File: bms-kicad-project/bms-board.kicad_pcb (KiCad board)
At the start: 4 copper layers, 218 parts, among them J1 12402012E212A, J2 DEBUG, J3 Conn_02x18_Odd_Even, J4 Conn_02x18_Odd_Even, Q1 BSS308PE_H6327, Q10 BSS308PE_H6327, Q11 BSS308PE_H6327, Q12 BSS308PE_H6327, Q13 BSS308PE_H6327, Q2 BSS308PE_H6327, Q3 BSS308PE_H6327, Q4 BSS308PE_H6327, Q5 BSS308PE_H6327, Q6 BSS308PE_H6327, Q7 BSS308PE_H6327, Q8 BSS308PE_H6327, Q9 BSS308PE_H6327, SW1 KMR223G LFG, SW2 KMR223G LFG, U1 LTC6804-2, U2 W25Q128JVSIQ TR, U3 NCP1117ST33T3G, U4 RP2040, U5 SIC461ED-T1-GE3, X1 ABM8-272-T3

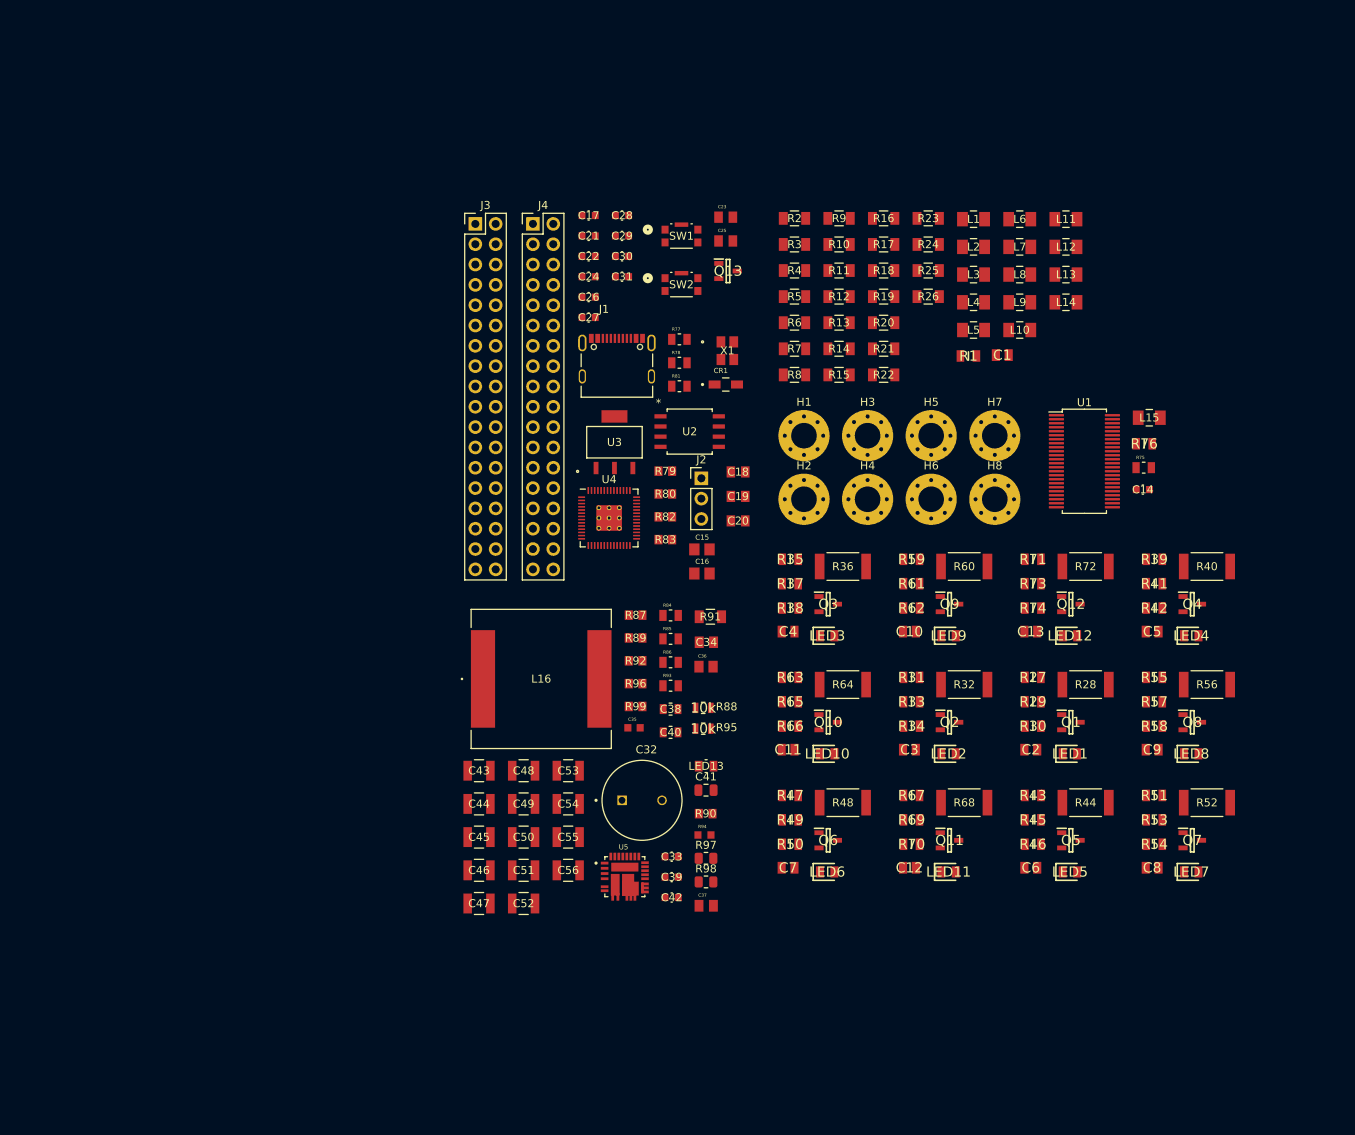
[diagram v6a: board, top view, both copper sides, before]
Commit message: Feature/current sensor (#17)
* feat: making sure my git still works

* feat: figured out battery stack monitor V+ biasing. Refer to task 5 on the punchlist for more details.

* feat: swapped out battery<->18V diode for cheaper alternative

* feat: started a new sheet for external connections and added current sensor

* feat: made a placeholder label to connect current sensor to LTC6811 GPIO

* feat: added remaining connectors to component library

* Wired up most external connections

* feat: Just shifting a few things around
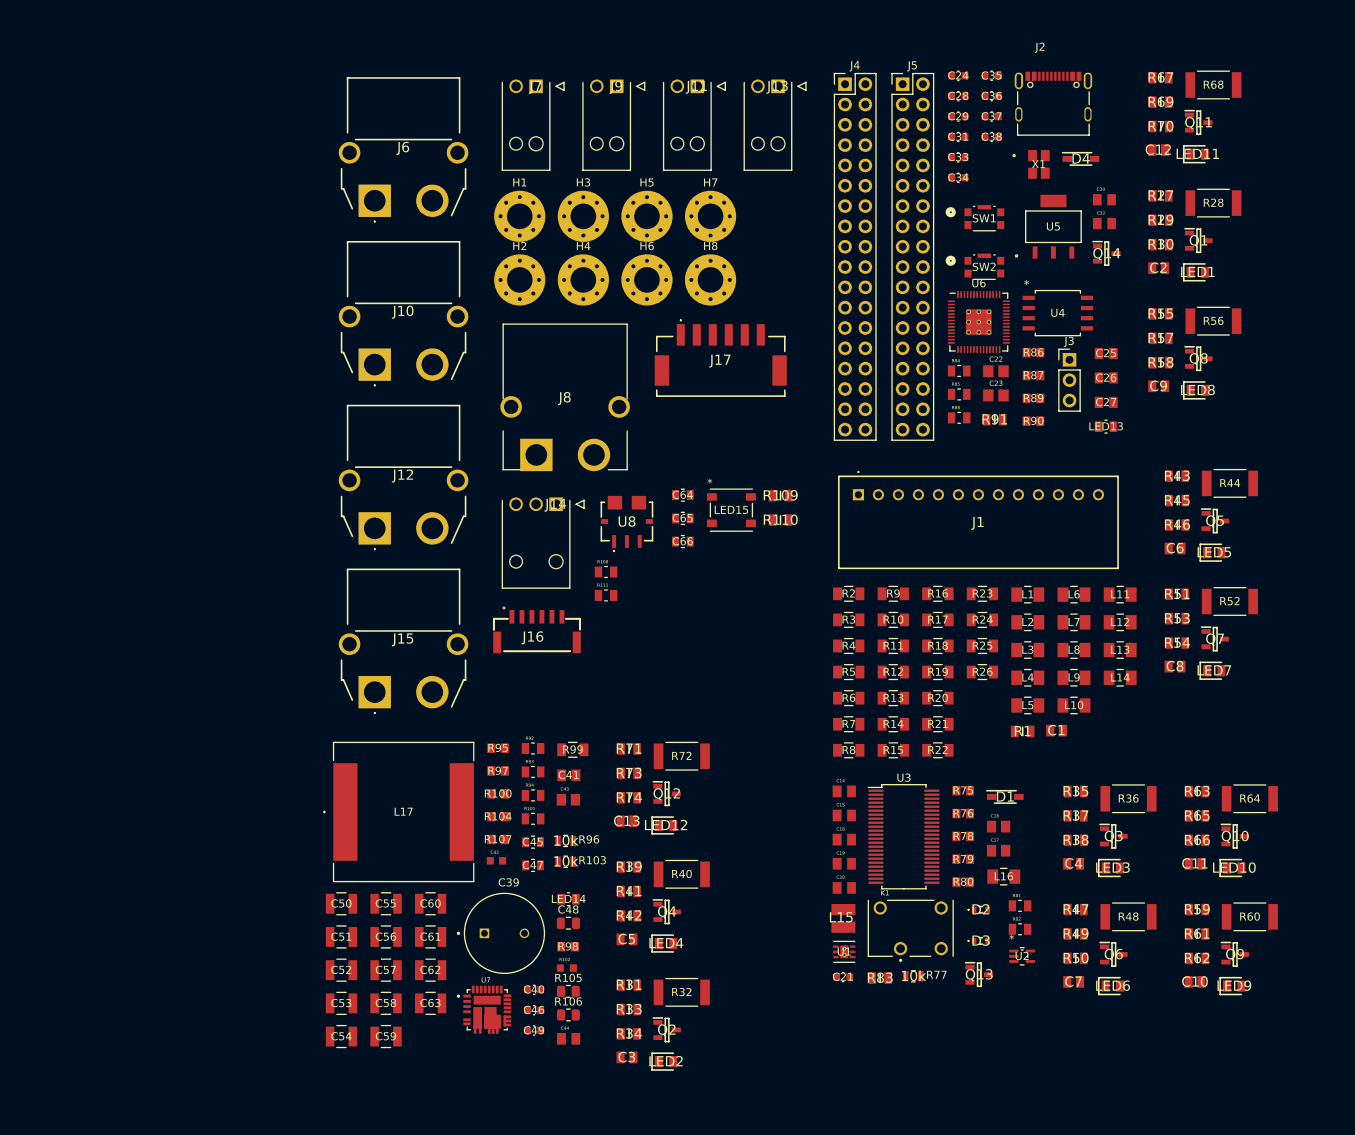
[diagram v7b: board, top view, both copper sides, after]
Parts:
- removed CR1: MBR120VLSFT1G, FixedWing:DIOM3616X98N
- added C57: 47u, FixedWing:G-32_MUR, F.Cu at (75.9, 148.3)
- added C58: 47u, FixedWing:G-32_MUR, F.Cu at (75.9, 152.5)
- added C59: 47u, FixedWing:G-32_MUR, F.Cu at (75.9, 156.6)
- added C60: 47u, FixedWing:G-32_MUR, F.Cu at (81.4, 140.0)
- added C61: 47u, FixedWing:G-32_MUR, F.Cu at (81.4, 144.2)
- added C62: 47u, FixedWing:G-32_MUR, F.Cu at (81.4, 148.3)
- added C63: 47u, FixedWing:G-32_MUR, F.Cu at (81.4, 152.5)
- added C64: 0.1µ, FixedWing:G-21_MUR, F.Cu at (113.0, 88.9)
- added C65: 1.5n, FixedWing:G-21_MUR, F.Cu at (113.0, 91.8)
- added C66: 0.1µ, FixedWing:G-21_MUR, F.Cu at (113.0, 94.7)
- added D1: B130LAW-7-F, FixedWing:SOD3716X145N, F.Cu at (153.3, 126.7)
- added D2: 1N4448X-TP, FixedWing:1N4448XTP, F.Cu at (150.2, 140.8)
- added D3: 1N4448X-TP, FixedWing:1N4448XTP, F.Cu at (150.2, 144.7)
- added D4: B130LAW-7-F, FixedWing:SOD3716X145N, F.Cu at (162.7, 46.9)
- added J10: XT60PW-F, FixedWing:XT60PWF, F.Cu at (74.5, 72.6)
- added J11: 1053131302, FixedWing:105313YY02, F.Cu at (114.8, 37.8)
- added J12: XT60PW-F, FixedWing:XT60PWF, F.Cu at (74.5, 93.1)
- added J13: 1053131302, FixedWing:105313YY02, F.Cu at (124.9, 37.8)
- added J14: 1053131303, FixedWing:105313YY03, F.Cu at (97.1, 90.1)
- added J15: XT60PW-F, FixedWing:XT60PWF, F.Cu at (74.5, 113.6)
- added J16: SM06B-GHS-TB, FixedWing:SM06B-GHS-TB, F.Cu at (89.4, 108.4)
- added J17: 5024940670, FixedWing:5024940670, F.Cu at (117.7, 72.7)
- added J5: Conn_02x18_Odd_Even, Connector_PinHeader_2.54mm:PinHeader_2x18_P2.54mm_Vertical, F.Cu at (140.4, 37.6)
- added J6: XT60PW-F, FixedWing:XT60PWF, F.Cu at (74.5, 52.1)
- added J7: 1053131302, FixedWing:105313YY02, F.Cu at (94.6, 37.8)
- added J8: XT60PW-M, FixedWing:XT60PWM, F.Cu at (98.3, 83.9)
- added J9: 1053131302, FixedWing:105313YY02, F.Cu at (104.7, 37.8)
- added K1: G6L-1P_DC5, FixedWing:RELAY_G6L-1P_DC5, F.Cu at (141.5, 143.1)
- added L17: 5.6u, FixedWing:IND_IHLP-6767GZ_VIS, F.Cu at (78.1, 128.5)
- added LED14: LTST-C170KGKT, FixedWing:LED_LTST-C170KGKT_LTO, F.Cu at (98.7, 139.4)
- added LED15: COM-16347, FixedWing:COM-16347_SPK, F.Cu at (119.0, 90.8)
- added Q14: BSS308PE_H6327, FixedWing:SOT95P260X110-3N, F.Cu at (166.0, 58.7)
- added R100: 1k, FixedWing:RC0805N_YAG, F.Cu at (89.9, 126.3)
- added R101: 93.1k, FixedWing:RESC2012X60N, F.Cu at (94.2, 129.4)
- added R102: 3.3, FixedWing:RESC1608X55N, F.Cu at (98.5, 148.0)
- added R103: 10k, FixedWing:KOA_Speer-RK73H2A-0-0-MFG, F.Cu at (98.3, 134.8)
- added R104: 11.5k, FixedWing:RC0805N_YAG, F.Cu at (89.9, 129.1)
- added R105: R, Resistor_SMD:R_0805_2012Metric, F.Cu at (98.7, 151.0)
- added R106: R, Resistor_SMD:R_0805_2012Metric, F.Cu at (98.7, 153.9)
- added R107: 56.2k, FixedWing:RC0805N_YAG, F.Cu at (89.9, 132.0)
- added R108: 5.6k, FixedWing:RESC2012X60N, F.Cu at (103.4, 98.5)
- added R109: 100, FixedWing:RESC2012X50N, F.Cu at (125.2, 89.0)
- added R110: 100, FixedWing:RESC2012X50N, F.Cu at (125.2, 92.1)
- added R111: 100k, FixedWing:RESC2012X60N, F.Cu at (103.4, 101.5)
- added U6: RP2040, FixedWing:RP2040-QFN-56, F.Cu at (150.0, 67.3)
- added U7: SIC461ED-T1-GE3, FixedWing:CONV_SIC461ED-T1-GE3, F.Cu at (88.5, 153.3)
- added U8: ACS72981KLRATR-150B5, FixedWing:ACS780LLRTR050BT, F.Cu at (106.0, 92.3)
- C14: value 0.1µ -> 4.7u; footprint FixedWing:CAP_GCJ-18_MUR -> FixedWing:CAPC2012X145N
- C15: value 15p -> 4.7u; footprint FixedWing:CAPC2012X70 -> FixedWing:CAPC2012X145N
- C16: value 15p -> 33n; footprint FixedWing:CAPC2012X70 -> FixedWing:CAPC2012X94N
- C17: value 0.1µ -> 33n; footprint FixedWing:CAP_GCJ-18_MUR -> FixedWing:CAPC2012X94N
- C18, C19, C20: value 10µ -> 4.7u; footprint FixedWing:CAP_CL21B106KOQNNNE_SAM -> FixedWing:CAPC2012X145N
- C22: value 0.1µ -> 15p; footprint FixedWing:CAP_GCJ-18_MUR -> FixedWing:CAPC2012X70
- C23: value 1µ -> 15p; footprint FixedWing:CAPC2012X140N -> FixedWing:CAPC2012X70
- C25: value 1µ -> 10µ; footprint FixedWing:CAPC2012X140N -> FixedWing:CAP_CL21B106KOQNNNE_SAM
- C26, C27: value 0.1µ -> 10µ; footprint FixedWing:CAP_GCJ-18_MUR -> FixedWing:CAP_CL21B106KOQNNNE_SAM
- C30: value 0.1µ -> 1µ; footprint FixedWing:CAP_GCJ-18_MUR -> FixedWing:CAPC2012X140N
- C32: value 220u -> 1µ; footprint FixedWing:CAPPRD500W60D1000H2500 -> FixedWing:CAPC2012X140N
- C34: value 560p -> 0.1µ; footprint FixedWing:CAP_CC0805_YAG -> FixedWing:CAP_GCJ-18_MUR
- C35: value 1u -> 0.1µ; footprint FixedWing:CAPC1608X90N -> FixedWing:CAP_GCJ-18_MUR
- C36: value 33n -> 0.1µ; footprint FixedWing:CAPC2012X94N -> FixedWing:CAP_GCJ-18_MUR
- C37: value 4.7u -> 0.1µ; footprint FixedWing:CAPC2012X145N -> FixedWing:CAP_GCJ-18_MUR
- C38: value 3.9n -> 0.1µ; footprint FixedWing:G-21_MUR -> FixedWing:CAP_GCJ-18_MUR
- C39: value 0.1µ -> 220u; footprint FixedWing:CAP_GCJ-18_MUR -> FixedWing:CAPPRD500W60D1000H2500
- C40: value 1.5n -> 0.1µ; footprint FixedWing:G-21_MUR -> FixedWing:CAP_GCJ-18_MUR
- C41: value C -> 560p; footprint Capacitor_SMD:C_0805_2012Metric -> FixedWing:CAP_CC0805_YAG
- C42: value 0.1µ -> 1u; footprint FixedWing:CAP_GCJ-18_MUR -> FixedWing:CAPC1608X90N
- C43: value 47u -> 33n; footprint FixedWing:G-32_MUR -> FixedWing:CAPC2012X94N
- C44: value 47u -> 4.7u; footprint FixedWing:G-32_MUR -> FixedWing:CAPC2012X145N
- C45: value 47u -> 3.9n; footprint FixedWing:G-32_MUR -> FixedWing:G-21_MUR
- C46, C49: value 47u -> 0.1µ; footprint FixedWing:G-32_MUR -> FixedWing:CAP_GCJ-18_MUR
- C47: value 47u -> 1.5n; footprint FixedWing:G-32_MUR -> FixedWing:G-21_MUR
- C48: value 47u -> C; footprint FixedWing:G-32_MUR -> Capacitor_SMD:C_0805_2012Metric
- J1: value 12402012E212A -> S13B-XH-A; footprint FixedWing:AMPHENOL_12402012E212A -> FixedWing:S13BXHALFSN
- J2: value DEBUG -> 12402012E212A; footprint Connector_PinHeader_2.54mm:PinHeader_1x03_P2.54mm_Vertical -> FixedWing:AMPHENOL_12402012E212A
- J3: value Conn_02x18_Odd_Even -> DEBUG; footprint Connector_PinHeader_2.54mm:PinHeader_2x18_P2.54mm_Vertical -> Connector_PinHeader_2.54mm:PinHeader_1x03_P2.54mm_Vertical
- L15: value 600Ω -> SDR0302-120ML; footprint FixedWing:IND_BLM31PG391SN1L_MUR -> FixedWing:SDR0302-471KL
- L16: value 5.6u -> 600Ω; footprint FixedWing:IND_IHLP-6767GZ_VIS -> FixedWing:IND_BLM31PG391SN1L_MUR
- R75: value 5.6k -> 56k2; footprint FixedWing:RESC2012X60N -> FixedWing:RC0805N_YAG
- R76: value 100 -> 33k2; footprint FixedWing:RESC2012X50N -> FixedWing:RC0805N_YAG
- R77: value 5.6k -> 10k; footprint FixedWing:RESC2012X60N -> FixedWing:KOA_Speer-RK73H2A-0-0-MFG
- R78: value 5.6k -> 33k2; footprint FixedWing:RESC2012X60N -> FixedWing:RC0805N_YAG
- R79: value 1k -> 11k5
- R80: value 1k -> 56k2
- R81: value 5.6k -> 100k
- R82: value 27 -> 5.6k; footprint FixedWing:RC0805N_YAG -> FixedWing:RESC2012X60N
- R83: value 27 -> 100; footprint FixedWing:RC0805N_YAG -> FixedWing:RESC2012X50N
- R84: value 562k -> 5.6k
- R85: value 100k -> 5.6k
- R86: value 100k -> 1k; footprint FixedWing:RESC2012X60N -> FixedWing:RC0805N_YAG
- R87: value 523k -> 1k
- R88: value 10k -> 5.6k; footprint FixedWing:KOA_Speer-RK73H2A-0-0-MFG -> FixedWing:RESC2012X60N
- R89: value 1k -> 27
- R90: value 41.2 -> 27; footprint FixedWing:RC0805N_VIS -> FixedWing:RC0805N_YAG
- R91: value 0 -> 475; footprint FixedWing:RC1206N_YAG -> FixedWing:RESC2012X50N
- R92: value 1k -> 562k; footprint FixedWing:RC0805N_YAG -> FixedWing:RESC2012X60N
- R93: value 93.1k -> 100k
- R94: value 3.3 -> 100k; footprint FixedWing:RESC1608X55N -> FixedWing:RESC2012X60N
- R95: value 10k -> 523k; footprint FixedWing:KOA_Speer-RK73H2A-0-0-MFG -> FixedWing:RC0805N_YAG
- R96: value 11.5k -> 10k; footprint FixedWing:RC0805N_YAG -> FixedWing:KOA_Speer-RK73H2A-0-0-MFG
- R97: value R -> 1k; footprint Resistor_SMD:R_0805_2012Metric -> FixedWing:RC0805N_YAG
- R98: value R -> 41.2; footprint Resistor_SMD:R_0805_2012Metric -> FixedWing:RC0805N_VIS
- R99: value 56.2k -> 0; footprint FixedWing:RC0805N_YAG -> FixedWing:RC1206N_YAG
- U1: value LTC6804-2 -> TPS61170DRVR; footprint FixedWing:SSOP-48_5.3x12.8mm_P0.5mm -> FixedWing:DRV6_1P6X1
- U2: value W25Q128JVSIQ TR -> SN74LVC1G17DCKR; footprint FixedWing:SOIC_208MIL_WIN -> FixedWing:DCK5
- U3: value NCP1117ST33T3G -> LTC6804-2; footprint FixedWing:SOT223-3_ONS -> FixedWing:SSOP-48_5.3x12.8mm_P0.5mm
- U4: value RP2040 -> W25Q128JVSIQ TR; footprint FixedWing:RP2040-QFN-56 -> FixedWing:SOIC_208MIL_WIN
- U5: value SIC461ED-T1-GE3 -> NCP1117ST33T3G; footprint FixedWing:CONV_SIC461ED-T1-GE3 -> FixedWing:SOT223-3_ONS
- moved C37 104.9 mm to (151.6, 41.6)
- moved C21 98.0 mm to (133.0, 149.2)
- moved U5 97.3 mm to (159.3, 55.4)
- moved C12 95.0 mm to (172.4, 45.8)
- moved LED11 95.0 mm to (177.3, 46.3)
- moved Q11 95.0 mm to (177.5, 42.4)
- moved R67 95.0 mm to (172.7, 36.8)
- moved R68 95.0 mm to (179.3, 37.7)
- moved R69 95.0 mm to (172.7, 39.8)
- moved R70 95.0 mm to (172.7, 42.9)
- moved C17 94.5 mm to (152.4, 133.4)
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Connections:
- C14 pad 1: Net-(U1-V+) -> GND
- C14 pad 2: GND -> Net-(U1-CTRL)
- C15 pad 2: /RP2040 Microcontroller/XIN -> Net-(U1-CTRL)
- C16 pad 1: GND -> Net-(C16-Pad1)
- C17 pad 1: +3V3 -> GND
- C17 pad 2: GND -> Net-(C16-Pad1)
- C18 pad 1: Net-(Q13-S) -> GND
- C18 pad 2: GND -> Net-(D1-K)
- C19 pad 2: +3V3 -> Net-(D1-K)
- C20 pad 2: +3V3 -> Net-(D1-K)
- C21 pad 1: GND -> Net-(U3-V+)
- C21 pad 2: +1V1 -> GND
- C22 pad 2: +1V1 -> /RP2040 Microcontroller/XIN
- C23 pad 2: +1V1 -> Net-(C23-Pad2)
- C25 pad 1: GND -> Net-(D4-K)
- C25 pad 2: +3V3 -> GND
- C26 pad 1: +3V3 -> GND
- C26 pad 2: GND -> +3V3
- C28 pad 1: +3V3 -> GND
- C28 pad 2: GND -> +1V1
- C29 pad 1: +3V3 -> GND
- C29 pad 2: GND -> +1V1
- C30 pad 1: +3V3 -> GND
- C30 pad 2: GND -> +1V1
- C32 pad 1: +BATT -> GND
- C32 pad 2: GND -> +3V3
- C33 pad 1: GND -> +3V3
- C33 pad 2: +BATT -> GND
- C34 pad 2: Net-(C34-Pad2) -> +3V3
- C35 pad 1: Net-(U5-VDD) -> +3V3
- C36 pad 1: GND -> +3V3
- C36 pad 2: Net-(U5-SS) -> GND
- C37 pad 1: GND -> +3V3
- C37 pad 2: Net-(U5-VDRV) -> GND
- C38 pad 1: Net-(U5-VSNS) -> +3V3
- C38 pad 2: Net-(C38-Pad2) -> GND
- C39 pad 1: Net-(C39-Pad1) -> +BATT
- C39 pad 2: Net-(U5-PHASE) -> GND
- C40 pad 1: Net-(C38-Pad2) -> GND
- C40 pad 2: +5V -> +BATT
- C41 pad 1: Net-(C41-Pad1) -> GND
- C41 pad 2: GND -> Net-(C41-Pad2)
- C42 pad 1: GND -> Net-(U7-VDD)
- C42 pad 2: +5V -> GND
- C43 pad 2: +5V -> Net-(U7-SS)
- C44 pad 2: +5V -> Net-(U7-VDRV)
- C45 pad 1: GND -> Net-(U7-VSNS)
- C45 pad 2: +5V -> Net-(C45-Pad2)
- C46 pad 1: GND -> Net-(C46-Pad1)
- C46 pad 2: +5V -> Net-(U7-PHASE)
- C47 pad 1: GND -> Net-(C45-Pad2)
- C48 pad 1: GND -> Net-(C48-Pad1)
- C48 pad 2: +5V -> GND
- J3 pad 1: GND -> /RP2040 Microcontroller/SWCLK
- J3 pad 2: +3V3 -> GND
- J3 pad 3: GND -> /RP2040 Microcontroller/SWD
- J4 pad 1: /RP2040 Microcontroller/GPIO29_ADC3 -> GND
- J4 pad 10: GND -> /RP2040 Microcontroller/GPIO3
- J4 pad 11: /RP2040 Microcontroller/GPIO24 -> GND
- J4 pad 12: GND -> /RP2040 Microcontroller/GPIO4
- J4 pad 13: /RP2040 Microcontroller/GPIO23 -> GND
- J4 pad 14: GND -> /RP2040 Microcontroller/GPIO5
- J4 pad 15: /RP2040 Microcontroller/GPIO22 -> GND
- J4 pad 16: GND -> /RP2040 Microcontroller/GPIO6
- J4 pad 17: /RP2040 Microcontroller/GPIO21 -> GND
- J4 pad 18: GND -> /RP2040 Microcontroller/GPIO7
- J4 pad 19: /RP2040 Microcontroller/GPIO20 -> GND
- J4 pad 2: GND -> +3V3
- J4 pad 20: GND -> /RP2040 Microcontroller/GPIO8
- J4 pad 21: /RP2040 Microcontroller/GPIO19 -> GND
- J4 pad 22: GND -> /RP2040 Microcontroller/GPIO9
- J4 pad 23: /RP2040 Microcontroller/GPIO18 -> GND
- J4 pad 24: GND -> /RP2040 Microcontroller/GPIO10
- J4 pad 25: /RP2040 Microcontroller/GPIO17 -> GND
- J4 pad 26: GND -> /RP2040 Microcontroller/GPIO11
- J4 pad 27: /RP2040 Microcontroller/GPIO16 -> GND
- J4 pad 28: GND -> /RP2040 Microcontroller/GPIO12
- J4 pad 29: /RP2040 Microcontroller/RUN -> GND
- J4 pad 3: /RP2040 Microcontroller/GPIO28_ADC2 -> GND
- J4 pad 30: GND -> /RP2040 Microcontroller/GPIO13
- J4 pad 31: /RP2040 Microcontroller/SWD -> GND
- J4 pad 32: GND -> /RP2040 Microcontroller/GPIO14
- J4 pad 33: /RP2040 Microcontroller/SWCLK -> GND
- J4 pad 34: GND -> /RP2040 Microcontroller/GPIO15
- J4 pad 4: GND -> /RP2040 Microcontroller/GPIO0
- J4 pad 5: /RP2040 Microcontroller/GPIO27_ADC1 -> GND
- J4 pad 6: GND -> /RP2040 Microcontroller/GPIO1
- J4 pad 7: /RP2040 Microcontroller/GPIO26_ADC0 -> GND
- J4 pad 8: GND -> /RP2040 Microcontroller/GPIO2
- J4 pad 9: /RP2040 Microcontroller/GPIO25 -> GND
- L1 pad 2: unconnected-(L1-Pad2) -> Net-(J1-Pad13)
- L10 pad 1: unconnected-(L10-Pad1) -> Net-(J1-Pad5)
- L11 pad 2: unconnected-(L11-Pad2) -> Net-(J1-Pad8)
- L12 pad 1: unconnected-(L12-Pad1) -> Net-(J1-Pad6)
- L13 pad 2: unconnected-(L13-Pad2) -> Net-(J1-Pad7)
- L14 pad 2: Net-(L14-Pad2) -> Net-(J1-Pad1)
- L15 pad 1: +BATT -> Net-(U1-CTRL)
- L15 pad 2: Net-(L15-Pad2) -> Net-(D1-A)
- L16 pad 1: Net-(U5-SW) -> Net-(L16-Pad1)
- L16 pad 2: +5V -> Net-(D2-K)
- L2 pad 1: Net-(L14-Pad2) -> Net-(J1-Pad1)
- L3 pad 2: unconnected-(L3-Pad2) -> Net-(J1-Pad12)
- L4 pad 1: unconnected-(L4-Pad1) -> Net-(J1-Pad2)
- L5 pad 2: unconnected-(L5-Pad2) -> Net-(J1-Pad11)
- L6 pad 1: unconnected-(L6-Pad1) -> Net-(J1-Pad3)
- L7 pad 2: unconnected-(L7-Pad2) -> Net-(J1-Pad10)
- L8 pad 1: unconnected-(L8-Pad1) -> Net-(J1-Pad4)
- L9 pad 2: unconnected-(L9-Pad2) -> Net-(J1-Pad9)
- Q13 pad 1: Net-(J1-VBUS) -> Net-(Q13-G)
- Q13 pad 2: Net-(Q13-S) -> +5V
- Q13 pad 3: +5V -> Net-(Q13-D)
- R1 pad 2: unconnected-(R1-Pad2) -> /Cell Filtering and Balancing/Filter and Balance Cell 12/C(n)
- R75 pad 1: /RP2040 Microcontroller/GPIO0 -> Net-(Q13-G)
- R75 pad 2: +5V -> +BATT
- R76 pad 1: Net-(U1-V+) -> GND
- R76 pad 2: Net-(L15-Pad2) -> Net-(Q13-G)
- R77 pad 2: Net-(J1-CC1_B) -> Net-(Q13-D)
- R78 pad 1: GND -> Net-(U1-COMP)
- R78 pad 2: Net-(J1-CC1_A) -> Net-(C16-Pad2)
- R79 pad 1: Net-(C16-Pad2) -> Net-(U1-FB)
- R79 pad 2: /RP2040 Microcontroller/XOUT -> Net-(D1-K)
- R80 pad 1: /RP2040 Microcontroller/~{USB_BOOT} -> Net-(R80-Pad1)
- R80 pad 2: /RP2040 Microcontroller/QSPI_SS -> Net-(U1-FB)
- R81 pad 1: +3V3 -> GND
- R81 pad 2: /RP2040 Microcontroller/~{RESET} -> Net-(R80-Pad1)
- R82 pad 1: Net-(U4-USB_DP) -> /RP2040 Microcontroller/GPIO0
- R82 pad 2: /RP2040 Microcontroller/USB_D+ -> +5V
- R83 pad 1: Net-(U4-USB_DM) -> Net-(U3-V+)
- R83 pad 2: /RP2040 Microcontroller/USB_D- -> Net-(L16-Pad1)
- R84 pad 1: Net-(U5-EN) -> GND
- R84 pad 2: +BATT -> Net-(J2-CC1_B)
- R85 pad 1: Net-(R85-Pad1) -> GND
- R85 pad 2: Net-(U5-EN) -> Net-(J2-CC1_A)
- R86 pad 1: GND -> Net-(C23-Pad2)
- R86 pad 2: Net-(R85-Pad1) -> /RP2040 Microcontroller/XOUT
- R87 pad 1: Net-(C34-Pad2) -> /RP2040 Microcontroller/~{USB_BOOT}
- R87 pad 2: Net-(U5-COMP) -> /RP2040 Microcontroller/QSPI_SS
- R88 pad 1: Net-(U5-VDD) -> +3V3
- R88 pad 2: Net-(LED13-A) -> /RP2040 Microcontroller/~{RESET}
- R89 pad 1: GND -> Net-(U6-USB_DP)
- R89 pad 2: Net-(R89-Pad2) -> /RP2040 Microcontroller/USB_D+
- R90 pad 1: GND -> Net-(U6-USB_DM)
- R90 pad 2: Net-(U5-ILIMIT) -> /RP2040 Microcontroller/USB_D-
- R91 pad 1: Net-(U5-VDD) -> /RP2040 Microcontroller/GPIO25
- R91 pad 2: Net-(U5-ULTRASONIC) -> Net-(LED13-A)
- R92 pad 1: Net-(R89-Pad2) -> Net-(U7-EN)
- R92 pad 2: Net-(U5-MODE) -> +BATT
- R93 pad 1: GND -> Net-(R93-Pad1)
- R93 pad 2: Net-(U5-FSW) -> Net-(U7-EN)
- R94 pad 1: Net-(U5-BOOT) -> GND
- R94 pad 2: Net-(C39-Pad1) -> Net-(R93-Pad1)
- R95 pad 1: GND -> Net-(C41-Pad2)
- R95 pad 2: Net-(U5-VFB) -> Net-(U7-COMP)
- R96 pad 1: Net-(U5-SW) -> Net-(U7-VDD)
- R96 pad 2: Net-(C38-Pad2) -> Net-(LED14-A)
- R97 pad 1: Net-(U5-SW) -> GND
- R97 pad 2: Net-(C41-Pad1) -> Net-(R100-Pad1)
- R98 pad 1: Net-(U5-SW) -> GND
- R98 pad 2: Net-(C41-Pad1) -> Net-(U7-ILIMIT)
- R99 pad 1: Net-(U5-VFB) -> Net-(U7-VDD)
- R99 pad 2: +5V -> Net-(U7-ULTRASONIC)
- U1 pad 1: Net-(U1-V+) -> Net-(U1-FB)
- U1 pad 2: /Battery Stack Monitor/C12 -> Net-(U1-COMP)
- U1 pad 3: /Battery Stack Monitor/S12 -> GND
- U1 pad 4: /Battery Stack Monitor/C11 -> Net-(D1-A)
- U1 pad 5: /Battery Stack Monitor/S11 -> Net-(U1-CTRL)
- U1 pad 6: /Battery Stack Monitor/C10 -> Net-(U1-CTRL)
- U1 pad 7: /Battery Stack Monitor/S10 -> GND
- U2 pad 1: /RP2040 Microcontroller/QSPI_SS -> unconnected-(U2-NC-Pad1)
- U2 pad 2: /RP2040 Microcontroller/QSPI_SD1 -> Net-(Q13-D)
- U2 pad 3: /RP2040 Microcontroller/QSPI_SD2 -> GND
- U2 pad 4: unconnected-(U2-GND-Pad4) -> /RP2040 Microcontroller/GPIO6
- U2 pad 5: /RP2040 Microcontroller/QSPI_SD0 -> +5V
- U3 pad 1: GND -> Net-(U3-V+)
- U3 pad 2: +3V3 -> /Battery Stack Monitor/C12
- U3 pad 3: Net-(Q13-S) -> /Battery Stack Monitor/S12
- U4 pad 1: unconnected-(U4-IOVDD-Pad1) -> /RP2040 Microcontroller/QSPI_SS
- U4 pad 2: /RP2040 Microcontroller/GPIO0 -> /RP2040 Microcontroller/QSPI_SD1
- U4 pad 3: /RP2040 Microcontroller/GPIO1 -> /RP2040 Microcontroller/QSPI_SD2
- U4 pad 4: /RP2040 Microcontroller/GPIO2 -> unconnected-(U4-GND-Pad4)
- U4 pad 5: /RP2040 Microcontroller/GPIO3 -> /RP2040 Microcontroller/QSPI_SD0
- U4 pad 6: /RP2040 Microcontroller/GPIO4 -> /RP2040 Microcontroller/QSPI_SCLK
- U4 pad 7: /RP2040 Microcontroller/GPIO5 -> /RP2040 Microcontroller/QSPI_SD3
- U4 pad 8: /RP2040 Microcontroller/GPIO6 -> +3V3
- U5 pad 1: +BATT -> GND
- U5 pad 2: Net-(LED13-A) -> +3V3
- U5 pad 3: Net-(U5-EN) -> Net-(D4-K)
- X1 pad 3: Net-(C16-Pad2) -> Net-(C23-Pad2)

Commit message: feat: don't even know what I changed, just zoned out for several hours. Made PCB r/a mount XT-60s and solder pads into a 2-for-1 deal
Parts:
- removed D3: 1N4448X-TP, FixedWing:1N4448XTP
- removed D4: B130LAW-7-F, FixedWing:SOD3716X145N
- removed K1: G6L-1P_DC5, FixedWing:RELAY_G6L-1P_DC5
- removed L10, L11, L12, L13, L14, L16, L2, L3, L4, L5, L6, L7, L8, L9: 600Ω, FixedWing:IND_BLM31PG391SN1L_MUR
- removed L15: SDR0302-120ML, FixedWing:SDR0302-471KL
- removed L17: 5.6u, FixedWing:IND_IHLP-6767GZ_VIS
- removed Q14: BSS308PE_H6327, FixedWing:SOT95P260X110-3N
- removed U8: ACS72981KLRATR-150B5, FixedWing:ACS780LLRTR050BT
- added C67: 0.1µ, FixedWing:CAP_GCJ-18_MUR, F.Cu at (75.3, 91.6)
- added J18: XT60PW-F, FixedWing:XT60PWF, F.Cu at (38.7, 127.5)
- added NT1: NetTie_2, NetTie:NetTie-2_SMD_Pad2.0mm, F.Cu at (137.1, 118.3)
- added NT2: NetTie_3, NetTie:NetTie-3_SMD_Pad2.0mm, F.Cu at (105.1, 160.7)
- added R112: 1k, FixedWing:RC0805N_YAG, F.Cu at (114.1, 155.1)
- added R113: 93.1k, FixedWing:RESC2012X60N, F.Cu at (118.5, 158.2)
- added R114: 3.3, FixedWing:RESC1608X55N, F.Cu at (118.3, 160.9)
- added R115: 10k, FixedWing:KOA_Speer-RK73H2A-0-0-MFG, F.Cu at (97.1, 165.5)
- added R116: 11.5k, FixedWing:RC0805N_YAG, F.Cu at (114.1, 158.0)
- added R117: R, Resistor_SMD:R_0805_2012Metric, F.Cu at (97.4, 151.4)
- added R118: R, Resistor_SMD:R_0805_2012Metric, F.Cu at (97.4, 154.3)
- added R119: 56.2k, FixedWing:RC0805N_YAG, F.Cu at (114.1, 160.8)
- added R120: 5.6k, FixedWing:RESC2012X60N, F.Cu at (89.4, 88.5)
- added R121: 100, FixedWing:RESC2012X50N, F.Cu at (89.4, 82.4)
- added R122: 100, FixedWing:RESC2012X50N, F.Cu at (89.4, 85.5)
- added R123: 100k, FixedWing:RESC2012X60N, F.Cu at (89.4, 91.4)
- added Z1: BZT52C5V6T-7, FixedWing:BZT52C5V6T7, F.Cu at (97.8, 65.3)
- added Z10: BZT52C5V6T-7, FixedWing:BZT52C5V6T7, F.Cu at (113.1, 65.3)
- added Z11: BZT52C5V6T-7, FixedWing:BZT52C5V6T7, F.Cu at (113.1, 69.2)
- added Z12: BZT52C5V6T-7, FixedWing:BZT52C5V6T7, F.Cu at (113.1, 73.1)
- added Z2: BZT52C5V6T-7, FixedWing:BZT52C5V6T7, F.Cu at (97.8, 69.2)
- added Z3: BZT52C5V6T-7, FixedWing:BZT52C5V6T7, F.Cu at (97.8, 73.1)
- added Z4: BZT52C5V6T-7, FixedWing:BZT52C5V6T7, F.Cu at (102.9, 65.3)
- added Z5: BZT52C5V6T-7, FixedWing:BZT52C5V6T7, F.Cu at (102.9, 69.2)
- added Z6: BZT52C5V6T-7, FixedWing:BZT52C5V6T7, F.Cu at (102.9, 73.1)
- added Z7: BZT52C5V6T-7, FixedWing:BZT52C5V6T7, F.Cu at (108.0, 65.3)
- added Z8: BZT52C5V6T-7, FixedWing:BZT52C5V6T7, F.Cu at (108.0, 69.2)
- added Z9: BZT52C5V6T-7, FixedWing:BZT52C5V6T7, F.Cu at (108.0, 73.1)
- C1, C10, C11, C12, C13, C2, C3, C4, C5, C6, C7, C8, C9: value 10n -> 0.1µ; footprint FixedWing:CAPC2012X95N -> FixedWing:CAP_GCJ-18_MUR
- C14, C15: value 4.7u -> 1u; footprint FixedWing:CAPC2012X145N -> FixedWing:CAP_CL31_SAM
- C16: value 33n -> 100p; footprint FixedWing:CAPC2012X94N -> FixedWing:CAPC220145_88N_KEM
- C17: value 33n -> 0.1µ; footprint FixedWing:CAPC2012X94N -> FixedWing:CAP_GCJ-18_MUR
- C18, C20: value 4.7u -> 0.1µ; footprint FixedWing:CAPC2012X145N -> FixedWing:CAP_GCJ-18_MUR
- C19: value 4.7u -> 100p; footprint FixedWing:CAPC2012X145N -> FixedWing:CAPC220145_88N_KEM
- C21: value 0.1µ -> 1u; footprint FixedWing:CAP_GCJ-18_MUR -> FixedWing:CAPC1608X90N
- C22: value 15p -> 1u; footprint FixedWing:CAPC2012X70 -> FixedWing:CAPC1608X90N
- C24: value 0.1µ -> 15p; footprint FixedWing:CAP_GCJ-18_MUR -> FixedWing:CAPC2012X70
- C25: value 10µ -> 0.1µ; footprint FixedWing:CAP_CL21B106KOQNNNE_SAM -> FixedWing:CAP_GCJ-18_MUR
- C28: value 0.1µ -> 10µ; footprint FixedWing:CAP_GCJ-18_MUR -> FixedWing:CAP_CL21B106KOQNNNE_SAM
- C30, C32: value 1µ -> 0.1µ; footprint FixedWing:CAPC2012X140N -> FixedWing:CAP_GCJ-18_MUR
- C31, C33: value 0.1µ -> 1µ; footprint FixedWing:CAP_GCJ-18_MUR -> FixedWing:CAPC1608X90N
- C39: value 220u -> 0.1µ; footprint FixedWing:CAPPRD500W60D1000H2500 -> FixedWing:CAP_GCJ-18_MUR
- C40: value 0.1µ -> 220u; footprint FixedWing:CAP_GCJ-18_MUR -> FixedWing:CAPPRD500W60D1000H2500
- C41: value 560p -> 0.1µ; footprint FixedWing:CAP_CC0805_YAG -> FixedWing:CAP_GCJ-18_MUR
- C42: value 1u -> 560p; footprint FixedWing:CAPC1608X90N -> FixedWing:CAP_CC0805_YAG
- C43: value 33n -> 1u; footprint FixedWing:CAPC2012X94N -> FixedWing:CAPC1608X90N
- C44: value 4.7u -> 33n; footprint FixedWing:CAPC2012X145N -> FixedWing:CAPC2012X94N
- C45: value 3.9n -> 4.7u; footprint FixedWing:G-21_MUR -> FixedWing:CAPC2012X145N
- C46: value 0.1µ -> 3.9n; footprint FixedWing:CAP_GCJ-18_MUR -> FixedWing:G-21_MUR
- C47: value 1.5n -> 0.1µ; footprint FixedWing:G-21_MUR -> FixedWing:CAP_GCJ-18_MUR
- C48: value C -> 1.5n; footprint Capacitor_SMD:C_0805_2012Metric -> FixedWing:G-21_MUR
- C49: value 0.1µ -> C; footprint FixedWing:CAP_GCJ-18_MUR -> Capacitor_SMD:C_0805_2012Metric
- C50: value 47u -> 0.1µ; footprint FixedWing:G-32_MUR -> FixedWing:CAP_GCJ-18_MUR
- C64: value 0.1µ -> 47u; footprint FixedWing:G-21_MUR -> FixedWing:G-32_MUR
- C66: footprint FixedWing:G-21_MUR -> FixedWing:CAP_GCJ-18_MUR
- D1: value B130LAW-7-F -> 100V; footprint FixedWing:SOD3716X145N -> FixedWing:D_SOD-123
- D2: value 1N4448X-TP -> 100V; footprint FixedWing:1N4448XTP -> FixedWing:D_SOD-123
- J11: value 1053131302 -> XT60PW-F; footprint FixedWing:105313YY02 -> FixedWing:XT60PWF
- J13: value 1053131302 -> XT60PW-F; footprint FixedWing:105313YY02 -> FixedWing:XT60PWF_Pad
- J14: value 1053131303 -> 1053131302; footprint FixedWing:105313YY03 -> FixedWing:105313YY02
- J15: value XT60PW-F -> 1053131302; footprint FixedWing:XT60PWF -> FixedWing:105313YY02
- J16: value SM06B-GHS-TB -> 1053131302; footprint FixedWing:SM06B-GHS-TB -> FixedWing:105313YY02
- J17: value 5024940670 -> 1053131302; footprint FixedWing:5024940670 -> FixedWing:105313YY02
- J6: value XT60PW-F -> XT60PW-M; footprint FixedWing:XT60PWF -> FixedWing:XT60PWM_Pad
- J7: value 1053131302 -> 5024940670; footprint FixedWing:105313YY02 -> FixedWing:5024940670
- J8: value XT60PW-M -> 1053131303; footprint FixedWing:XT60PWM -> FixedWing:105313YY03
- J9: value 1053131302 -> SM06B-GHS-TB; footprint FixedWing:105313YY02 -> FixedWing:SM06B-GHS-TB
- L1: value 600Ω -> 5.6u; footprint FixedWing:IND_BLM31PG391SN1L_MUR -> FixedWing:IND_IHLP-6767GZ_VIS
- Q1, Q10, Q11, Q12, Q2, Q3, Q4, Q5, Q6, Q7, Q8, Q9: value BSS308PE_H6327 -> DNBT8105-7; footprint FixedWing:SOT95P260X110-3N -> FixedWing:SOT95P240X105-3N
- R10, R15, R20, R25, R5: value 0 -> 475; footprint FixedWing:RC1206N_YAG -> FixedWing:RESC2012X50N
- R100: value 1k -> 5.6k; footprint FixedWing:RC0805N_YAG -> FixedWing:RESC2012X60N
- R101: value 93.1k -> 27; footprint FixedWing:RESC2012X60N -> FixedWing:RC0805N_YAG
- R102: value 3.3 -> 27; footprint FixedWing:RESC1608X55N -> FixedWing:RC0805N_YAG
- R103: value 10k -> 475; footprint FixedWing:KOA_Speer-RK73H2A-0-0-MFG -> FixedWing:RESC2012X50N
- R104: value 11.5k -> 562k; footprint FixedWing:RC0805N_YAG -> FixedWing:RESC2012X60N
- R105, R106: value R -> 100k; footprint Resistor_SMD:R_0805_2012Metric -> FixedWing:RESC2012X60N
- R107: value 56.2k -> 523k
- R108: value 5.6k -> 10k; footprint FixedWing:RESC2012X60N -> FixedWing:KOA_Speer-RK73H2A-0-0-MFG
- R109: value 100 -> 1k; footprint FixedWing:RESC2012X50N -> FixedWing:RC0805N_YAG
- R11, R16, R21, R26, R6: value 0 -> 100; footprint FixedWing:RC1206N_YAG -> FixedWing:RESC2012X50N
- R110: value 100 -> 41.2; footprint FixedWing:RESC2012X50N -> FixedWing:RC0805N_VIS
- R111, R81: value 100k -> 0; footprint FixedWing:RESC2012X60N -> FixedWing:RC1206N_YAG
- R12, R17, R2, R22, R7: value 0 -> 27; footprint FixedWing:RC1206N_YAG -> FixedWing:RC0805N_YAG
- R13, R14, R18, R19, R23, R24, R3, R4, R8, R9: value 0 -> 15; footprint FixedWing:RC1206N_YAG -> FixedWing:RES_R1632_ROM
- R27, R47: value 475 -> 27; footprint FixedWing:RESC2012X50N -> FixedWing:RC0805N_YAG
- R28, R44, R48: value 33 -> 15; footprint FixedWing:RC2512N_VIS -> FixedWing:RES_R1632_ROM
- R29, R33, R49, R53: value 100 -> 15; footprint FixedWing:RESC2012X50N -> FixedWing:RES_R1632_ROM
- R30, R50: value 3.3k -> 475
- R31, R51: value 475 -> 100
- R32, R52: value 33 -> 27; footprint FixedWing:RC2512N_VIS -> FixedWing:RC0805N_YAG
- R34, R38, R54, R58: value 3.3k -> 15; footprint FixedWing:RESC2012X50N -> FixedWing:RES_R1632_ROM
- R36, R56: value 33 -> 100; footprint FixedWing:RC2512N_VIS -> FixedWing:RESC2012X50N
- R37, R57: value 100 -> 27; footprint FixedWing:RESC2012X50N -> FixedWing:RC0805N_YAG
- R39, R43, R59: value 475 -> 15; footprint FixedWing:RESC2012X50N -> FixedWing:RES_R1632_ROM
- R40, R60: value 33 -> 475; footprint FixedWing:RC2512N_VIS -> FixedWing:RESC2012X50N
- R42: value 3.3k -> 27; footprint FixedWing:RESC2012X50N -> FixedWing:RC0805N_YAG
- R45: value 100 -> 475
- R46: value 3.3k -> 100
- R62, R66, R70: value 3.3k -> 10k; footprint FixedWing:RESC2012X50N -> FixedWing:KOA_Speer-RK73H2A-0-0-MFG
- R63, R67, R91: value 475 -> 10k; footprint FixedWing:RESC2012X50N -> FixedWing:KOA_Speer-RK73H2A-0-0-MFG
- R64, R68: value 33 -> 10k; footprint FixedWing:RC2512N_VIS -> FixedWing:KOA_Speer-RK73H2A-0-0-MFG
- R65, R69: value 100 -> 10k; footprint FixedWing:RESC2012X50N -> FixedWing:KOA_Speer-RK73H2A-0-0-MFG
- R71: value 475 -> 0; footprint FixedWing:RESC2012X50N -> FixedWing:RC1206N_YAG
- R72: value 33 -> 0; footprint FixedWing:RC2512N_VIS -> FixedWing:RC1206N_YAG
- R73, R83: value 100 -> 0; footprint FixedWing:RESC2012X50N -> FixedWing:RC1206N_YAG
- R74: value 3.3k -> 0; footprint FixedWing:RESC2012X50N -> FixedWing:RC1206N_YAG
- R75: value 56k2 -> 0; footprint FixedWing:RC0805N_YAG -> FixedWing:RC1206N_YAG
- R76, R78: value 33k2 -> 0; footprint FixedWing:RC0805N_YAG -> FixedWing:RC1206N_YAG
- R77: value 10k -> 0; footprint FixedWing:KOA_Speer-RK73H2A-0-0-MFG -> FixedWing:RC1206N_YAG
- R79: value 11k5 -> 0; footprint FixedWing:RC0805N_YAG -> FixedWing:RC1206N_YAG
- R80: value 56k2 -> 100; footprint FixedWing:RC0805N_YAG -> FixedWing:RESC2012X50N
- R82, R84, R85, R88: value 5.6k -> 0; footprint FixedWing:RESC2012X60N -> FixedWing:RC1206N_YAG
- R86, R87: value 1k -> 0; footprint FixedWing:RC0805N_YAG -> FixedWing:RC1206N_YAG
- R89: value 27 -> 0; footprint FixedWing:RC0805N_YAG -> FixedWing:RC1206N_YAG
- R90: value 27 -> 100; footprint FixedWing:RC0805N_YAG -> FixedWing:RESC2012X50N
- R92: value 562k -> 0.5m; footprint FixedWing:RESC2012X60N -> FixedWing:RES_3920R
- R93: value 100k -> 100; footprint FixedWing:RESC2012X60N -> FixedWing:RESC2012X50N
- R94: value 100k -> 1k; footprint FixedWing:RESC2012X60N -> FixedWing:RC0805N_YAG
- R95: value 523k -> 5.6k; footprint FixedWing:RC0805N_YAG -> FixedWing:RESC2012X60N
- R96: value 10k -> 5.6k; footprint FixedWing:KOA_Speer-RK73H2A-0-0-MFG -> FixedWing:RESC2012X60N
- R98: value 41.2 -> 1k; footprint FixedWing:RC0805N_VIS -> FixedWing:RC0805N_YAG
- R99: value 0 -> 10k; footprint FixedWing:RC1206N_YAG -> FixedWing:KOA_Speer-RK73H2A-0-0-MFG
- U1: value TPS61170DRVR -> CD74HC4067M; footprint FixedWing:DRV6_1P6X1 -> FixedWing:SOIC-24W_7.5x15.4mm_P1.27mm
- U2: value SN74LVC1G17DCKR -> BQ7697202PFBR; footprint FixedWing:DCK5 -> FixedWing:QFP50P900X900X120-48N
- U3: value LTC6804-2 -> W25Q128JVSIQ TR; footprint FixedWing:SSOP-48_5.3x12.8mm_P0.5mm -> FixedWing:SOIC_208MIL_WIN
- U4: value W25Q128JVSIQ TR -> NCP1117ST33T3G; footprint FixedWing:SOIC_208MIL_WIN -> FixedWing:SOT223-3_ONS
- U5: value NCP1117ST33T3G -> RP2040; footprint FixedWing:SOT223-3_ONS -> FixedWing:RP2040-QFN-56
- U6: value RP2040 -> SIC461ED-T1-GE3; footprint FixedWing:RP2040-QFN-56 -> FixedWing:CONV_SIC461ED-T1-GE3
- U7: value SIC461ED-T1-GE3 -> ACS72981KLRATR-150B5; footprint FixedWing:CONV_SIC461ED-T1-GE3 -> FixedWing:ACS780LLRTR050BT
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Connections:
- net /RP2040 Microcontroller/RUN renamed /Microcontroller/RUN
- C1 pad 1: /Cell Filtering and Balancing/Filter and Balance Cell 1/C(n-1) -> GND
- C1 pad 2: GND -> /Battery Stack Monitor/C0
- C10 pad 1: /Cell Filtering and Balancing/Filter and Balance Cell 10/C(n-1) -> /Battery Stack Monitor/C8
- C10 pad 2: /Cell Filtering and Balancing/Filter and Balance Cell 8/C(n) -> /Battery Stack Monitor/C9
- C11 pad 1: /Cell Filtering and Balancing/Filter and Balance Cell 10/C(n) -> /Battery Stack Monitor/C9
- C11 pad 2: /Cell Filtering and Balancing/Filter and Balance Cell 10/C(n-1) -> /Battery Stack Monitor/C10
- C12 pad 1: /Cell Filtering and Balancing/Filter and Balance Cell 11/C(n) -> /Battery Stack Monitor/C10
- C12 pad 2: /Cell Filtering and Balancing/Filter and Balance Cell 10/C(n) -> /Battery Stack Monitor/C11
- C13 pad 1: /Cell Filtering and Balancing/Filter and Balance Cell 12/C(n) -> /Battery Stack Monitor/C11
- C13 pad 2: /Cell Filtering and Balancing/Filter and Balance Cell 11/C(n) -> /Battery Stack Monitor/C12
- C14 pad 2: Net-(U1-CTRL) -> Net-(U2-BAT)
- C15 pad 2: Net-(U1-CTRL) -> Net-(U2-BAT)
- C16 pad 1: Net-(C16-Pad1) -> GND
- C16 pad 2: Net-(C16-Pad2) -> Net-(U2-BAT)
- C17 pad 1: GND -> Net-(U2-SRP)
- C17 pad 2: Net-(C16-Pad1) -> GND
- C18 pad 1: GND -> Net-(U2-SRP)
- C18 pad 2: Net-(D1-K) -> Net-(U2-SRN)
- C19 pad 1: GND -> Net-(U2-SRN)
- C19 pad 2: Net-(D1-K) -> Net-(U2-SRP)
- C2 pad 1: /Cell Filtering and Balancing/Filter and Balance Cell 1/C(n) -> GND
- C2 pad 2: /Cell Filtering and Balancing/Filter and Balance Cell 1/C(n-1) -> /Battery Stack Monitor/C1
- C20 pad 1: GND -> Net-(U2-SRN)
- C20 pad 2: Net-(D1-K) -> GND
- C21 pad 1: Net-(U3-V+) -> Net-(U2-REG18)
- C22 pad 1: GND -> Net-(U2-REG18)
- C22 pad 2: /RP2040 Microcontroller/XIN -> GND
- C23 pad 2: Net-(C23-Pad2) -> /Microcontroller/XIN
- C24 pad 1: +3V3 -> GND
- C24 pad 2: GND -> Net-(C24-Pad2)
- C25 pad 1: Net-(D4-K) -> +3V3
- C26 pad 1: GND -> Net-(Q13-S)
- C26 pad 2: +3V3 -> GND
- C28 pad 2: +1V1 -> +3V3
- C3 pad 1: /Cell Filtering and Balancing/Filter and Balance Cell 2/C(n) -> /Battery Stack Monitor/C1
- C3 pad 2: /Cell Filtering and Balancing/Filter and Balance Cell 1/C(n) -> /Battery Stack Monitor/C2
- C31 pad 1: +3V3 -> GND
- C31 pad 2: GND -> +1V1
- C32 pad 1: GND -> +3V3
- C32 pad 2: +3V3 -> GND
- C33 pad 1: +3V3 -> GND
- C33 pad 2: GND -> +3V3
- C34 pad 1: GND -> +3V3
- C34 pad 2: +3V3 -> GND
- C35 pad 1: +3V3 -> GND
- C35 pad 2: GND -> +3V3
- C39 pad 1: +BATT -> +3V3
- C4 pad 1: /Cell Filtering and Balancing/Filter and Balance Cell 3/C(n) -> /Battery Stack Monitor/C2
- C4 pad 2: /Cell Filtering and Balancing/Filter and Balance Cell 2/C(n) -> /Battery Stack Monitor/C3
- C40 pad 1: GND -> +BATT
- C40 pad 2: +BATT -> GNDPWR
- C41 pad 1: GND -> GNDPWR
- C41 pad 2: Net-(C41-Pad2) -> +BATT
- C42 pad 1: Net-(U7-VDD) -> GNDA
- C42 pad 2: GND -> Net-(C42-Pad2)
- C43 pad 1: GND -> Net-(U6-VDD)
- C43 pad 2: Net-(U7-SS) -> GNDA
- C44 pad 1: GND -> GNDA
- C44 pad 2: Net-(U7-VDRV) -> Net-(U6-SS)
- C45 pad 1: Net-(U7-VSNS) -> GNDPWR
- C45 pad 2: Net-(C45-Pad2) -> Net-(U6-VDRV)
- C46 pad 1: Net-(C46-Pad1) -> Net-(U6-VSNS)
- C46 pad 2: Net-(U7-PHASE) -> Net-(C46-Pad2)
- C47 pad 1: Net-(C45-Pad2) -> Net-(C47-Pad1)
- C47 pad 2: +5V -> Net-(U6-PHASE)
- C48 pad 1: Net-(C48-Pad1) -> Net-(C46-Pad2)
- C48 pad 2: GND -> +5V
- C49 pad 1: GND -> Net-(C49-Pad1)
- C49 pad 2: +5V -> GNDPWR
- C5 pad 1: /Cell Filtering and Balancing/Filter and Balance Cell 4/C(n) -> /Battery Stack Monitor/C3
- C5 pad 2: /Cell Filtering and Balancing/Filter and Balance Cell 3/C(n) -> /Battery Stack Monitor/C4
- C50 pad 1: GND -> GNDPWR
- C51 pad 1: GND -> GNDPWR
- C52 pad 1: GND -> GNDPWR
- C53 pad 1: GND -> GNDPWR
- C54 pad 1: GND -> GNDPWR
- C55 pad 1: GND -> GNDPWR
- C56 pad 1: GND -> GNDPWR
- C57 pad 1: GND -> GNDPWR
- C58 pad 1: GND -> GNDPWR
- C59 pad 1: GND -> GNDPWR
- C6 pad 1: /Cell Filtering and Balancing/Filter and Balance Cell 5/C(n) -> /Battery Stack Monitor/C4
- C6 pad 2: /Cell Filtering and Balancing/Filter and Balance Cell 4/C(n) -> /Battery Stack Monitor/C5
- C60 pad 1: GND -> GNDPWR
- C61 pad 1: GND -> GNDPWR
- C62 pad 1: GND -> GNDPWR
- C63 pad 1: GND -> GNDPWR
- C64 pad 1: GND -> GNDPWR
- C7 pad 1: /Cell Filtering and Balancing/Filter and Balance Cell 6/C(n) -> /Battery Stack Monitor/C5
- C7 pad 2: /Cell Filtering and Balancing/Filter and Balance Cell 5/C(n) -> /Battery Stack Monitor/C6
- C8 pad 1: /Cell Filtering and Balancing/Filter and Balance Cell 7/C(n) -> /Battery Stack Monitor/C6
- C8 pad 2: /Cell Filtering and Balancing/Filter and Balance Cell 6/C(n) -> /Battery Stack Monitor/C7
- C9 pad 1: /Cell Filtering and Balancing/Filter and Balance Cell 8/C(n) -> /Battery Stack Monitor/C7
- C9 pad 2: /Cell Filtering and Balancing/Filter and Balance Cell 7/C(n) -> /Battery Stack Monitor/C8
- D1 pad 1: Net-(D1-K) -> Net-(D1-Pad1)
- D1 pad 2: Net-(D1-A) -> +BATT
- D2 pad 1: Net-(D2-K) -> Net-(Q13-S)
- D2 pad 2: +BATT -> Net-(J2-VBUS)
- J1 pad 1: Net-(J1-Pad1) -> Net-(Q1-E)
- J1 pad 10: Net-(J1-Pad10) -> Net-(Q10-E)
- J1 pad 11: Net-(J1-Pad11) -> Net-(Q11-E)
- J1 pad 12: Net-(J1-Pad12) -> Net-(Q12-E)
- J1 pad 2: Net-(J1-Pad2) -> Net-(Q2-E)
- J1 pad 3: Net-(J1-Pad3) -> Net-(Q3-E)
- J1 pad 4: Net-(J1-Pad4) -> Net-(Q4-E)
- J1 pad 5: Net-(J1-Pad5) -> Net-(Q5-E)
- J1 pad 6: Net-(J1-Pad6) -> Net-(Q6-E)
- J1 pad 7: Net-(J1-Pad7) -> Net-(Q7-E)
- J1 pad 8: Net-(J1-Pad8) -> Net-(Q8-E)
- J1 pad 9: Net-(J1-Pad9) -> Net-(Q9-E)
- J10 pad 2: GND -> /Battery Stack Monitor/GNDCUR
- J11 pad 1: +5V -> +BATT
- J11 pad 2: GND -> /Battery Stack Monitor/GNDCUR
- J12 pad 2: GND -> /Battery Stack Monitor/GNDCUR
- J13 pad 1: +5V -> +BATT
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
